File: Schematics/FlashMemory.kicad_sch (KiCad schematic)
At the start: 4 parts, among them U8 W25Q128JVP

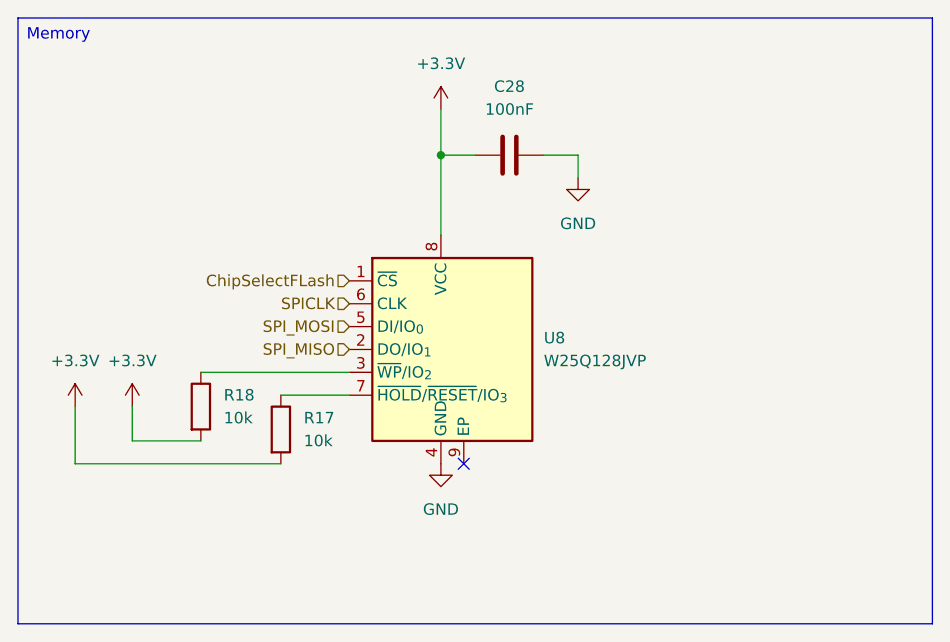
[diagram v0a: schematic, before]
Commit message: first layout need to go over schematic
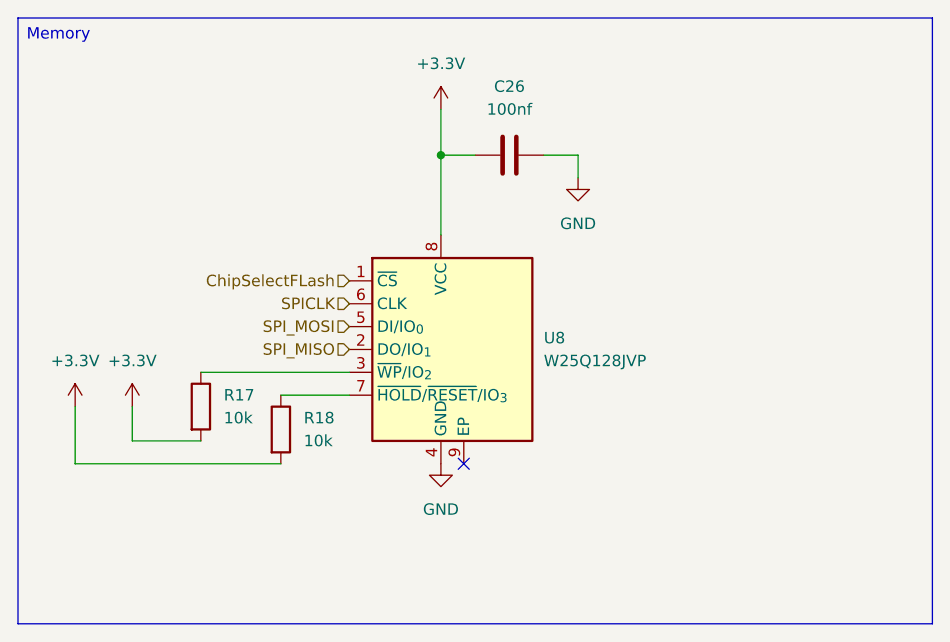
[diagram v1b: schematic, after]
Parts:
- C26: renamed from C28; value 100nF -> 100nf; footprint Capacitor_SMD:C_0201_0603Metric -> Capacitor_SMD:C_0805_2012Metric_Pad1.18x1.45mm_HandSolder; LCSC Part (none) -> C49678
- R17: renamed from R18; footprint (none) -> Resistor_SMD:R_0805_2012Metric_Pad1.20x1.40mm_HandSolder; LCSC Part (none) -> C84376
- R18: renamed from R17; footprint (none) -> Resistor_SMD:R_0805_2012Metric_Pad1.20x1.40mm_HandSolder; LCSC Part (none) -> C84376
- U8: LCSC Part (none) -> C190862
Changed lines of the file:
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@@
+			)
+		)
+		(property "LCSC Part" "C190862"
+			(at 127 85.09 0)
+			(effects
+				(font
+					(size 1.27 1.27)
+				)
+				(hide yes)
 			)
 		)
@@
 		(dnp no)
 		(fields_autoplaced yes)
-		(property "Reference" "C28"
+		(property "Reference" "C26"
 			(at 134.62 55.88 90)
 			(effects
@@
 			)
 		)
-		(property "Value" "100nF"
+		(property "Value" "100nf"
 			(at 134.62 58.42 90)
 			(effects
@@
 			)
 		)
-		(property "Footprint" "Capacitor_SMD:C_0201_0603Metric"
+		(property "Footprint" "Capacitor_SMD:C_0805_2012Metric_Pad1.18x1.45mm_HandSolder"
 			(at 138.43 62.5348 0)
 			(effects
@@
 			)
 		)
+		(property "LCSC Part" "C49678"
+			(at 134.62 63.5 90)
+			(effects
+				(font
+					(size 1.27 1.27)
+				)
+				(hide yes)
+			)
+		)
 		(pin "1"
 		)
@@
 			(project "flightcomputer2"
 				(path "/6cb3dda3-5fe8-4715-b831-354360aa3199/4f36624f-94d6-4603-9d4c-20df28968169"
-					(reference "C28")
+					(reference "C26")
 					(unit 1)
 				)
@@
 		(dnp no)
 		(fields_autoplaced yes)
-		(property "Reference" "R17"
+		(property "Reference" "R18"
 			(at 111.76 92.7099 0)
 			(effects
@@
 			)
 		)
-		(property "Footprint" ""
+		(property "Footprint" "Resistor_SMD:R_0805_2012Metric_Pad1.20x1.40mm_HandSolder"
 			(at 107.442 93.98 90)
 			(effects
@@
 			)
 		)
+		(property "LCSC Part" "C84376"
+			(at 109.22 93.98 0)
+			(effects
+				(font
+					(size 1.27 1.27)
+				)
+				(hide yes)
+			)
+		)
 		(pin "1"
 		)
@@
 			(project ""
 				(path "/6cb3dda3-5fe8-4715-b831-354360aa3199/4f36624f-94d6-4603-9d4c-20df28968169"
-					(reference "R17")
+					(reference "R18")
 					(unit 1)
 				)
@@
 		(dnp no)
 		(fields_autoplaced yes)
-		(property "Reference" "#PWR087"
+		(property "Reference" "#PWR088"
 			(at 142.24 72.39 0)
 			(effects
@@
 			(project "flightcomputer2"
 				(path "/6cb3dda3-5fe8-4715-b831-354360aa3199/4f36624f-94d6-4603-9d4c-20df28968169"
-					(reference "#PWR087")
+					(reference "#PWR088")
 					(unit 1)
 				)
@@
 		(dnp no)
 		(fields_autoplaced yes)
-		(property "Reference" "#PWR086"
+		(property "Reference" "#PWR087"
 			(at 127 104.14 0)
 			(effects
@@
 			(project "flightcomputer2"
 				(path "/6cb3dda3-5fe8-4715-b831-354360aa3199/4f36624f-94d6-4603-9d4c-20df28968169"
-					(reference "#PWR086")
+					(reference "#PWR087")
 					(unit 1)
 				)
@@
 		(dnp no)
 		(fields_autoplaced yes)
-		(property "Reference" "#PWR089"
+		(property "Reference" "#PWR085"
 			(at 92.71 95.25 0)
 			(effects
@@
 			(project "flightcomputer2"
 				(path "/6cb3dda3-5fe8-4715-b831-354360aa3199/4f36624f-94d6-4603-9d4c-20df28968169"
-					(reference "#PWR089")
+					(reference "#PWR085")
 					(unit 1)
 				)
@@
 		(dnp no)
 		(fields_autoplaced yes)
-		(property "Reference" "#PWR085"
+		(property "Reference" "#PWR086"
 			(at 127 62.23 0)
 			(effects
@@
 			(project "flightcomputer2"
 				(path "/6cb3dda3-5fe8-4715-b831-354360aa3199/4f36624f-94d6-4603-9d4c-20df28968169"
-					(reference "#PWR085")
+					(reference "#PWR086")
 					(unit 1)
 				)
@@
 		(dnp no)
 		(fields_autoplaced yes)
-		(property "Reference" "#PWR088"
+		(property "Reference" "#PWR084"
 			(at 86.36 95.25 0)
 			(effects
@@
 			(project ""
 				(path "/6cb3dda3-5fe8-4715-b831-354360aa3199/4f36624f-94d6-4603-9d4c-20df28968169"
-					(reference "#PWR088")
+					(reference "#PWR084")
 					(unit 1)
 				)
@@
 		(dnp no)
 		(fields_autoplaced yes)
-		(property "Reference" "R18"
+		(property "Reference" "R17"
 			(at 102.87 90.1699 0)
 			(effects
@@
 			)
 		)
-		(property "Footprint" ""
+		(property "Footprint" "Resistor_SMD:R_0805_2012Metric_Pad1.20x1.40mm_HandSolder"
 			(at 98.552 91.44 90)
 			(effects
@@
 			)
 		)
+		(property "LCSC Part" "C84376"
+			(at 100.33 91.44 0)
+			(effects
+				(font
+					(size 1.27 1.27)
+				)
+				(hide yes)
+			)
+		)
 		(pin "1"
 		)
@@
 			(project "flightcomputer2"
 				(path "/6cb3dda3-5fe8-4715-b831-354360aa3199/4f36624f-94d6-4603-9d4c-20df28968169"
-					(reference "R18")
-					(unit 1)
-				)
+					(reference "R17")
+					(unit 1)
+				)
